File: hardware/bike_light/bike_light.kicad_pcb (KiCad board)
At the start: 2 copper layers, 65 x 22 mm, 54 parts, among them J1 Battery, J2 USB_C_Receptacle_USB2.0_16P, SW1 SW_Push, SW2 SW_Push, U1 TPS22918DBV, U2 ESP32-C3-WROOM-02, U3 XC6220B331MR, U4 BQ21040DBV

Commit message: Moved USB connector to bottom from side
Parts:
- moved J2 38.3 mm to (95.7, 111.0), turned to 90 degrees
- moved R5 31.8 mm to (102.9, 112.2)
- moved R6 29.0 mm to (102.9, 109.2)
- moved J1 16.8 mm to (111.5, 118.9), turned to 0 degrees
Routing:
- net VBUS: track 43.9 -> 76.3 mm, vias 2 -> 3
- net GND: track 86.8 -> 56.0 mm, vias 36 -> 19
- net +3.3V: track 126.0 -> 103.0 mm
- net /USB_D-: track 37.7 -> 60.3 mm, vias 0 -> 2
- net +BATT: track 51.8 -> 70.5 mm, vias 0 -> 4
- net /USB_D+: track 45.0 -> 62.6 mm
- net /UART_TX: track 53.1 -> 70.5 mm
- net /IO8_STRAP: track 23.1 -> 8.24 mm, vias 2 -> 0
- net /LED_EN: track 68.9 -> 61.9 mm, vias 0 -> 2
- net /LED_VDD: track 97.7 -> 104.5 mm, vias 3 -> 2
- net /VBAT_SENSE: track 25.0 -> 21.0 mm, vias 0 -> 2
- net /CHG_STAT: track 69.0 -> 67.2 mm, vias 3 -> 2
- net /LED_CLK: track 13.4 -> 14.7 mm
- net /CHG_ISET: track 5.52 -> 4.58 mm
- net /UART_RX: track 51.4 -> 50.6 mm, vias 3 -> 1
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- added copper zone on F.Cu, net GND
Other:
- board size 65 x 22 mm -> 72 x 22 mm

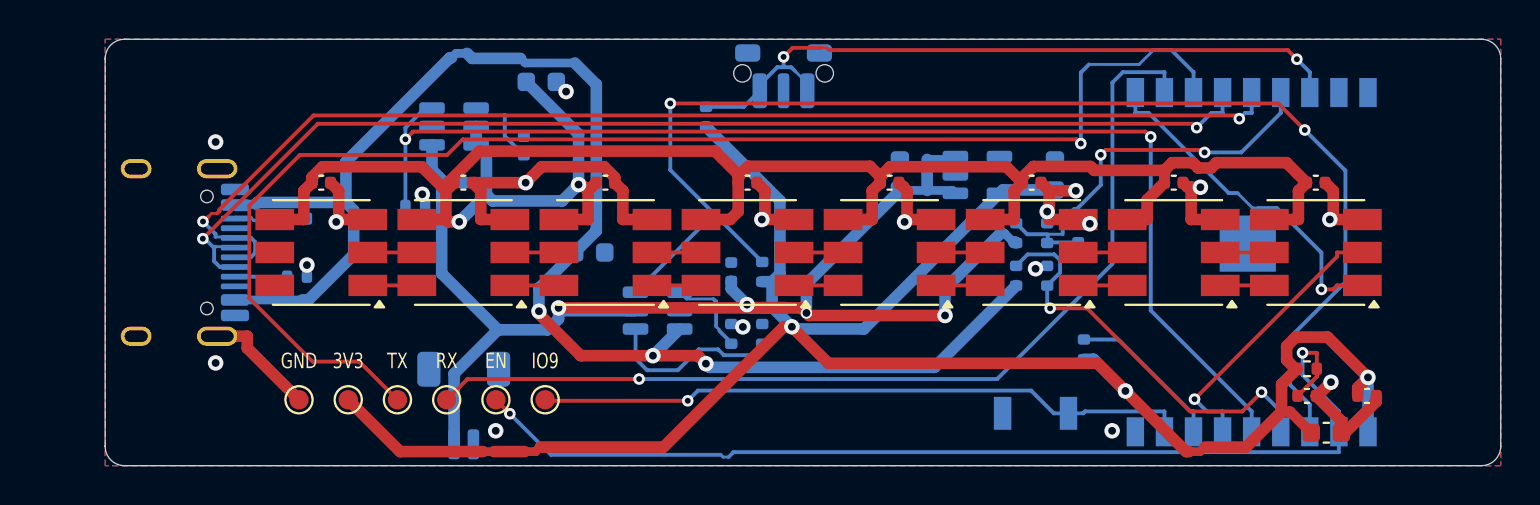
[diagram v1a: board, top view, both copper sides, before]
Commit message: Switched to ESP32-C3-MINI-1, shrunk board
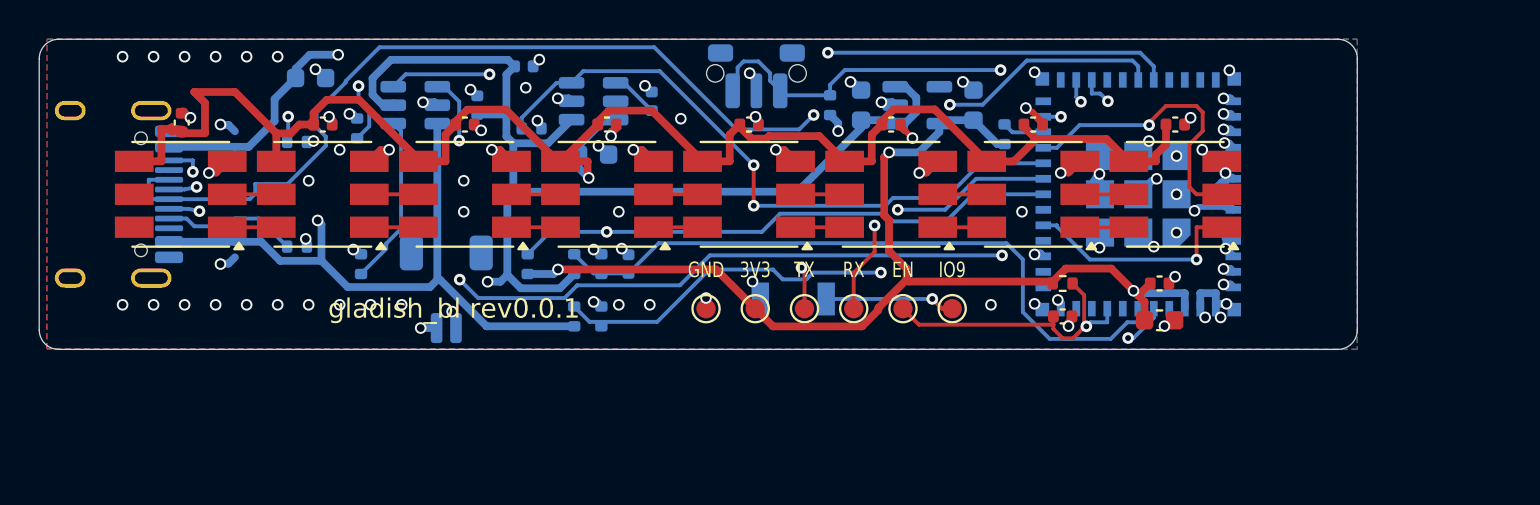
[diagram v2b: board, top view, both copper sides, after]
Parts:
- U2: value ESP32-C3-WROOM-02 -> ESP32-C3-MINI-1; footprint bike_light:ESP32-C3-WROOM-02_NoVias -> bike_light:ESP32-C3-MINI-1
- moved C19 23.3 mm to (120.0, 111.6)
- moved R13 23.1 mm to (118.6, 114.3)
- moved R11 23.1 mm to (118.6, 111.6)
- moved R12 22.9 mm to (117.2, 114.3)
- moved R10 22.9 mm to (117.2, 111.6)
- moved R7 22.0 mm to (106.0, 104.6)
- moved TP4 21.5 mm to (129.1, 113.9)
- moved TP1 21.5 mm to (126.5, 113.9)
- moved TP2 21.5 mm to (134.2, 113.9)
- moved TP5 21.5 mm to (131.6, 113.9)
- moved TP6 21.5 mm to (124.0, 113.9)
- moved TP3 21.5 mm to (136.7, 113.9)
- moved R8 21.0 mm to (106.2, 111.6)
- moved C17 17.0 mm to (103.6, 102.0)
- moved U4 16.4 mm to (109.0, 103.4)
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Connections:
- U2 pad 1: +3.3V -> GND
- U2 pad 10: /LED_DATA -> unconnected-(U2-NC-Pad10)
- U2 pad 11: /UART_RX -> GND
- U2 pad 12: /UART_TX -> unconnected-(U2-GPIO0/ADC1_CH0/XTAL_32K_P-Pad12)
- U2 pad 13: /USB_D- -> unconnected-(U2-GPIO1/ADC1_CH1/XTAL_32K_N-Pad13)
- U2 pad 14: /USB_D+ -> GND
- U2 pad 15: /VBAT_SENSE -> unconnected-(U2-NC-Pad15)
- U2 pad 16: /BUTTON -> /LED_DATA
- U2 pad 18: unconnected-(U2-IO0-Pad18) -> /CHG_STAT
- U2 pad 19: GND -> /VBUS_DET
- U2 pad 2: /ESP_EN -> GND
- U2 pad 3: /CHG_STAT -> +3.3V
- U2 pad 4: /VBUS_DET -> unconnected-(U2-NC-Pad4)
- U2 pad 5: /LED_EN -> /BUTTON
- U2 pad 6: /LED_CLK -> /VBAT_SENSE
- U2 pad 7: /IO8_STRAP -> unconnected-(U2-NC-Pad7)
- U2 pad 8: /BOOT -> /ESP_EN
- U2 pad 9: GND -> unconnected-(U2-NC-Pad9)
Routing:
- net +3.3V: track 103.0 -> 59.3 mm, vias 3 -> 4
- net /ESP_EN: track 54.1 -> 15.3 mm, vias 2 -> 1
- net /UART_TX: track 70.5 -> 34.0 mm, vias 1 -> 2
- net /LED_EN: track 61.9 -> 33.5 mm
- net /UART_RX: track 50.6 -> 24.1 mm, vias 1 -> 2
- net /CHG_STAT: track 67.2 -> 44.1 mm
- net VBUS: track 76.3 -> 55.0 mm, vias 3 -> 2
- net /LED_VDD: track 104.5 -> 84.8 mm, vias 2 -> 1
- net /VBAT_SENSE: track 21.0 -> 35.0 mm, vias 2 -> 0
- net /BOOT: track 33.8 -> 19.8 mm, vias 1 -> 2
- net /CHG_ISET: track 4.58 -> 13.0 mm, vias 0 -> 2
- net +BATT: track 70.5 -> 62.1 mm, vias 4 -> 2
- net /VBUS_DET: track 21.4 -> 29.6 mm
- net Net-(J2-CC2): track 2.82 -> 9.25 mm, vias 0 -> 2
- net /LED_DATA: track 17.7 -> 11.6 mm
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- added copper zone on In1.Cu, net GND
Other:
- board size 72 x 22 mm -> 68 x 16 mm
- copper layers 2 -> 4

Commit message: Claude re-layout
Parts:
- moved R9 24.5 mm to (139.0, 108.0), turned to 0 degrees
- moved R10 16.2 mm to (133.4, 110.6)
- moved R11 16.0 mm to (134.6, 110.6)
- moved C19 15.8 mm to (135.8, 110.6)
- moved R13 14.6 mm to (104.1, 112.4)
- moved R12 14.4 mm to (102.9, 112.4)
- moved R8 10.7 mm to (108.6, 101.2), turned to 0 degrees
- moved C16 9.91 mm to (138.3, 113.3)
- moved U3 9.91 mm to (135.3, 113.3)
- moved C15 9.90 mm to (132.3, 113.3)
- moved C1 5.41 mm to (111.6, 105.9)
- moved R1 5.38 mm to (110.6, 101.5), turned to 180 degrees
- moved C2 4.59 mm to (116.9, 101.6)
- moved U1 4.00 mm to (114.2, 103.3)
- moved C18 3.60 mm to (108.6, 103.4)
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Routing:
- net GND: track 59.8 -> 102.9 mm, vias 95 -> 46
- net VBUS: track 55.0 -> 24.5 mm
- net /VBAT_SENSE: track 35.0 -> 13.7 mm, vias 0 -> 2
- net +BATT: track 62.1 -> 43.4 mm
- net /CHG_ISET: track 13.0 -> 0.85 mm, vias 2 -> 0
- net /VBUS_DET: track 29.6 -> 40.6 mm
- net /BUTTON: track 38.0 -> 28.0 mm
- net /UART_TX: track 34.0 -> 24.3 mm, vias 2 -> 3
- net /CHG_STAT: track 44.1 -> 34.8 mm
- net /CHG_TS: track 8.78 -> 1.14 mm
- net /LED_VDD: track 84.8 -> 92.2 mm
- net +3.3V: track 59.3 -> 53.9 mm
- net Net-(J2-CC2): track 9.25 -> 5.19 mm, vias 2 -> 0
- net /USB_D+: track 62.0 -> 58.0 mm
- net /BOOT: track 19.8 -> 22.9 mm
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- added copper zone on In2.Cu, net GND
